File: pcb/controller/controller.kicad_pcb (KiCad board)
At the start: 2 copper layers, 153.8 x 101 mm, 21 parts, among them J1 USB_C_Receptacle, SW1 SW_Push, SW2 SW_Push, SW3 SW_Push, SW4 SW_Push, SW5 SW_Push, SW6 SW_Push, SW7 SW_Push, SW8 SW_Push

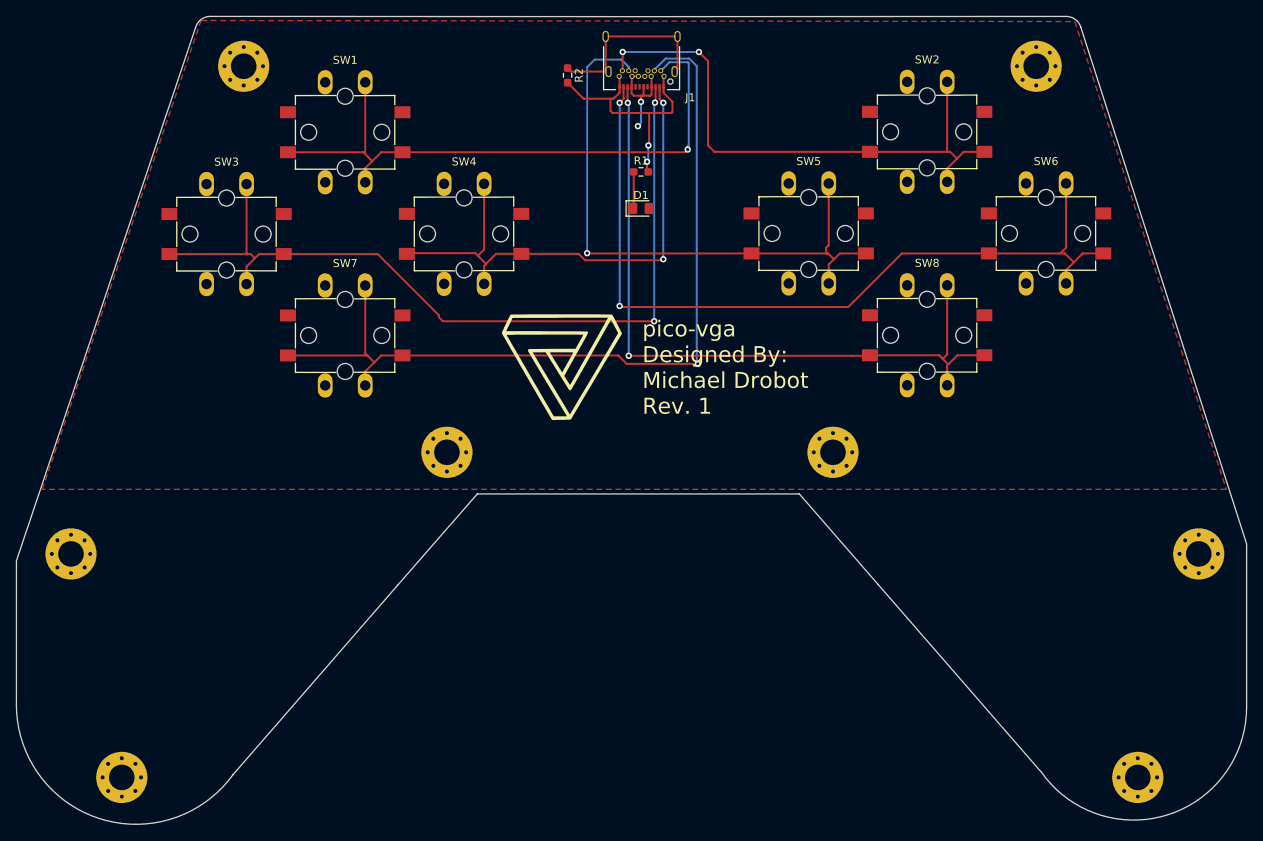
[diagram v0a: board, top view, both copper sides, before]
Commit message: Controller rev 2
 - Using an attiny24 and I2C now to communicate between the mainboard and the controllers
   - Gets rid of the massive multiplexer on the mainboard, simplifies things
   - Attiny software will probably be written in arduino because I'm lazy
 - Swapped the connector for a cheaper one since we don't need all 24 pins, still using usb-c though
 - Button layout stays the same
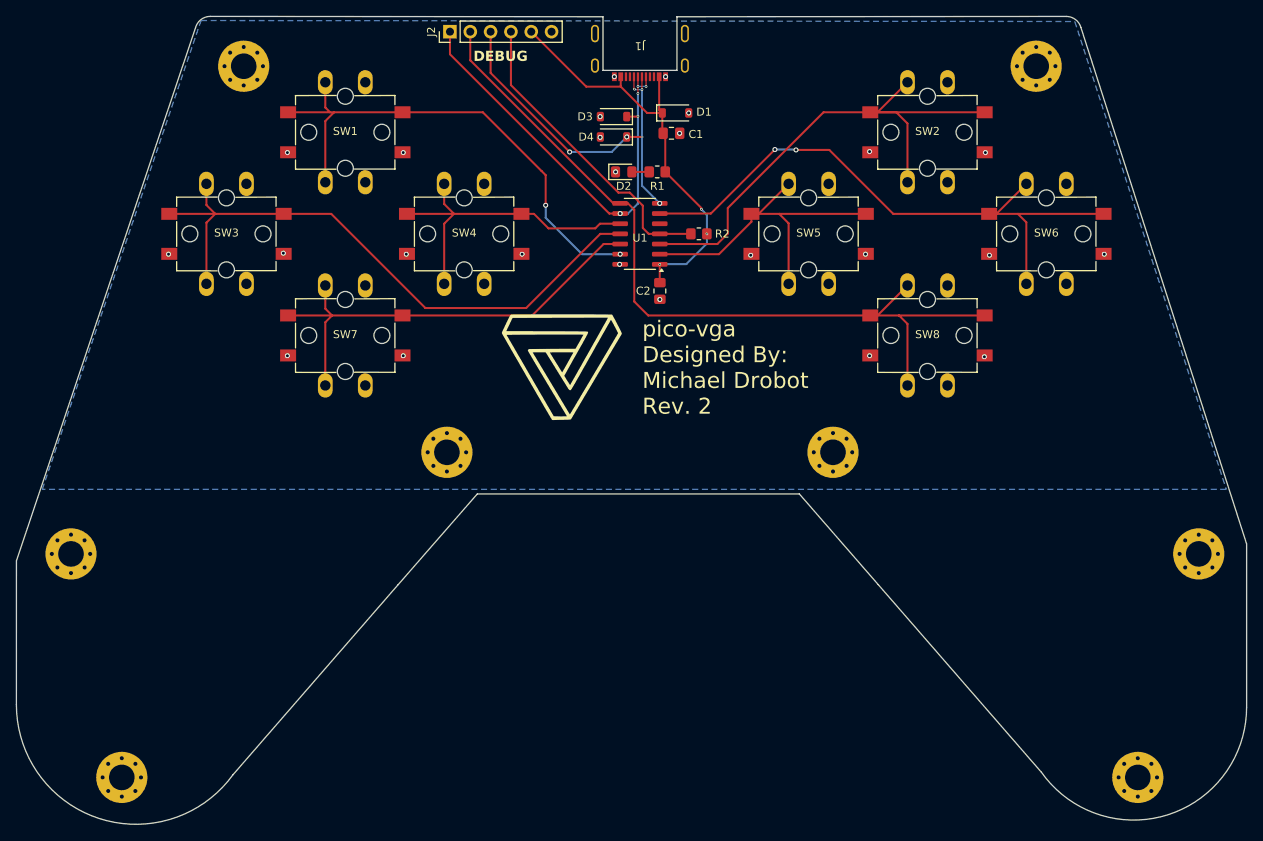
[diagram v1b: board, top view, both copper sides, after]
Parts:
- added C1: 10u, Capacitor_SMD:C_0805_2012Metric_Pad1.18x1.45mm_HandSolder, F.Cu at (96.6, 28.7)
- added C2: 100n, Capacitor_SMD:C_0805_2012Metric_Pad1.18x1.45mm_HandSolder, F.Cu at (95.2, 48.4)
- added D2: LED, LED_SMD:LED_0805_2012Metric_Pad1.15x1.40mm_HandSolder, F.Cu at (90.7, 33.5)
- added D3: 3.6V, Diode_SMD:D_SOD-123, F.Cu at (89.4, 26.6)
- added D4: 3.6V, Diode_SMD:D_SOD-123, F.Cu at (89.4, 29.2)
- added J2: Conn_01x06_Pin, Connector_PinHeader_2.54mm:PinHeader_1x06_P2.54mm_Vertical, F.Cu at (69.0, 16.0)
- added U1: ATtiny24A-SS, Package_SO:SOIC-14_3.9x8.7mm_P1.27mm, F.Cu at (92.7, 41.3)
- D1: value LED -> 3.6V; footprint LED_SMD:LED_0805_2012Metric_Pad1.15x1.40mm_HandSolder -> Diode_SMD:D_SOD-123
- J1: value USB_C_Receptacle -> USB_C_Receptacle_USB2.0_16P; footprint controller:USB_C_Receptacle_Molex_2171830001 -> controller:USB_C_Receptacle_Molex_2169900003
- R1: value 1K -> 4.7K; footprint Resistor_SMD:R_0603_1608Metric_Pad0.98x0.95mm_HandSolder -> Resistor_SMD:R_0805_2012Metric_Pad1.20x1.40mm_HandSolder
- R2: value 1M -> 4.7k; footprint Resistor_SMD:R_0603_1608Metric_Pad0.98x0.95mm_HandSolder -> Resistor_SMD:R_0805_2012Metric_Pad1.20x1.40mm_HandSolder
- moved R2 25.7 mm to (100.1, 41.3), turned to 0 degrees
- moved D1 12.7 mm to (97.2, 26.2)
- moved J1 3.75 mm to (92.7, 14.1)
- moved R1 2.03 mm to (94.9, 33.5)
- moved SW2 0.06 mm to (128.7, 28.6)
- moved SW6 0.06 mm to (143.5, 41.3)
- moved SW5 0.05 mm to (113.8, 41.3)
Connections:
- D1 pad 1: Net-(D1-Pad1) -> +3V3
- D1 pad 2: +3V3 -> GND
- J1 pad A6: +3V3 -> /MOSI
- J1 pad A7: unconnected-(J1-PadA7) -> /SCK
- J1 pad B6: +3V3 -> /MOSI
- J1 pad B7: unconnected-(J1-PadB7) -> /SCK
- J1 pad S1: Net-(J1-PadS1) -> GND
- R1 pad 1: GND -> +3V3
- R1 pad 2: Net-(D1-Pad1) -> Net-(D2-A)
- R2 pad 1: Net-(J1-PadS1) -> /RST
- R2 pad 2: GND -> +3V3
- SW1 pad 1: +3V3 -> /BTN_UP
- SW1 pad 2: Net-(J1-PadB11) -> GND
- SW2 pad 1: +3V3 -> /BTN_Y
- SW2 pad 2: Net-(J1-PadB2) -> GND
- SW3 pad 1: +3V3 -> /BTN_LEFT
- SW3 pad 2: Net-(J1-PadA3) -> GND
- SW4 pad 1: +3V3 -> /BTN_RIGHT
- SW4 pad 2: Net-(J1-PadA2) -> GND
- SW5 pad 1: +3V3 -> /BTN_X
- SW5 pad 2: Net-(J1-PadB3) -> GND
- SW6 pad 1: +3V3 -> /BTN_B
- SW6 pad 2: Net-(J1-PadA11) -> GND
- SW7 pad 1: +3V3 -> /BTN_DOWN
- SW7 pad 2: Net-(J1-PadB10) -> GND
- SW8 pad 1: +3V3 -> /BTN_A
- SW8 pad 2: Net-(J1-PadA10) -> GND
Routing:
- net Net-(J1-PadB10): track 108.3 -> 0.00 mm, vias 1 -> 0
- net Net-(J1-PadA3): track 106.5 -> 0.00 mm, vias 2 -> 0
- net Net-(J1-PadA11): track 103.9 -> 0.00 mm, vias 2 -> 0
- net /BTN_A: track 0.00 -> 103.2 mm
- net Net-(J1-PadA10): track 91.2 -> 0.00 mm, vias 2 -> 0
- net /BTN_LEFT: track 0.00 -> 78.5 mm
- net Net-(J1-PadB11): track 77.8 -> 0.00 mm, vias 1 -> 0
- net /BTN_B: track 0.00 -> 77.5 mm, vias 0 -> 2
- net Net-(J1-PadB3): track 77.3 -> 0.00 mm, vias 1 -> 0
- net Net-(J1-PadB2): track 71.8 -> 0.00 mm, vias 2 -> 0
- net /BTN_Y: track 0.00 -> 68.1 mm
- net Net-(J1-PadA2): track 67.2 -> 0.00 mm, vias 2 -> 0
- net /BTN_UP: track 0.00 -> 65.2 mm, vias 0 -> 2
- net /BTN_DOWN: track 0.00 -> 58.4 mm
- net /SCK: track 0.00 -> 54.6 mm, vias 0 -> 5
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- added copper zone on B.Cu, net GND
- removed copper zone on F.Cu, net +3V3
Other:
- outline, holes or cut-outs redrawn
- board text added: "DEBUG"
- board text added: "SCK MISO MOSI RST 3V3 GND"
- board text added: "pico-vga Designed By: Michael Drobot Rev. 2"
- board text removed: "pico-vga Designed By: Michael Drobot Rev. 1"
